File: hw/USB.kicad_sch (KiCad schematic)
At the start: 3 parts

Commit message: setup components information
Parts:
- R? (x2): footprint (none) -> Resistor_SMD:R_0805_2012Metric_Pad1.20x1.40mm_HandSolder; LCSC (none) -> C27834; Vendor (none) -> UNI-ROYAL(厚声); Vendor Model (none) -> 0805W8F5101T5E
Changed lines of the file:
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@@
       (effects (font (size 1.27 1.27)))
     )
-    (property "Footprint" "" (at 196.85 75.438 90)
+    (property "Footprint" "Resistor_SMD:R_0805_2012Metric_Pad1.20x1.40mm_HandSolder" (at 196.85 75.438 90)
       (effects (font (size 1.27 1.27)) hide)
     )
     (property "Datasheet" "~" (at 196.85 73.66 0)
+      (effects (font (size 1.27 1.27)) hide)
+    )
+    (property "Description" "电阻类型: 厚膜电阻 阻值: 5.1kΩ 精度: ±1% 功率: 1/8W 温度系数: ±100ppm/℃ 最大工作电压: 150V 工作温度" (at 196.85 73.66 0)
+      (effects (font (size 1.27 1.27)) hide)
+    )
+    (property "LCSC" "C27834" (at 196.85 73.66 0)
+      (effects (font (size 1.27 1.27)) hide)
+    )
+    (property "Vendor" "UNI-ROYAL(厚声)" (at 196.85 73.66 0)
+      (effects (font (size 1.27 1.27)) hide)
+    )
+    (property "Vendor Model" "0805W8F5101T5E" (at 196.85 73.66 0)
       (effects (font (size 1.27 1.27)) hide)
     )
@@
       (effects (font (size 1.27 1.27)))
     )
-    (property "Footprint" "" (at 196.85 88.138 90)
+    (property "Footprint" "Resistor_SMD:R_0805_2012Metric_Pad1.20x1.40mm_HandSolder" (at 196.85 88.138 90)
       (effects (font (size 1.27 1.27)) hide)
     )
@@
       (effects (font (size 1.27 1.27)) hide)
     )
+    (property "Description" "电阻类型: 厚膜电阻 阻值: 5.1kΩ 精度: ±1% 功率: 1/8W 温度系数: ±100ppm/℃ 最大工作电压: 150V 工作温度" (at 196.85 86.36 0)
+      (effects (font (size 1.27 1.27)) hide)
+    )
+    (property "LCSC" "C27834" (at 196.85 86.36 0)
+      (effects (font (size 1.27 1.27)) hide)
+    )
+    (property "Vendor" "UNI-ROYAL(厚声)" (at 196.85 86.36 0)
+      (effects (font (size 1.27 1.27)) hide)
+    )
+    (property "Vendor Model" "0805W8F5101T5E" (at 196.85 86.36 0)
+      (effects (font (size 1.27 1.27)) hide)
+    )

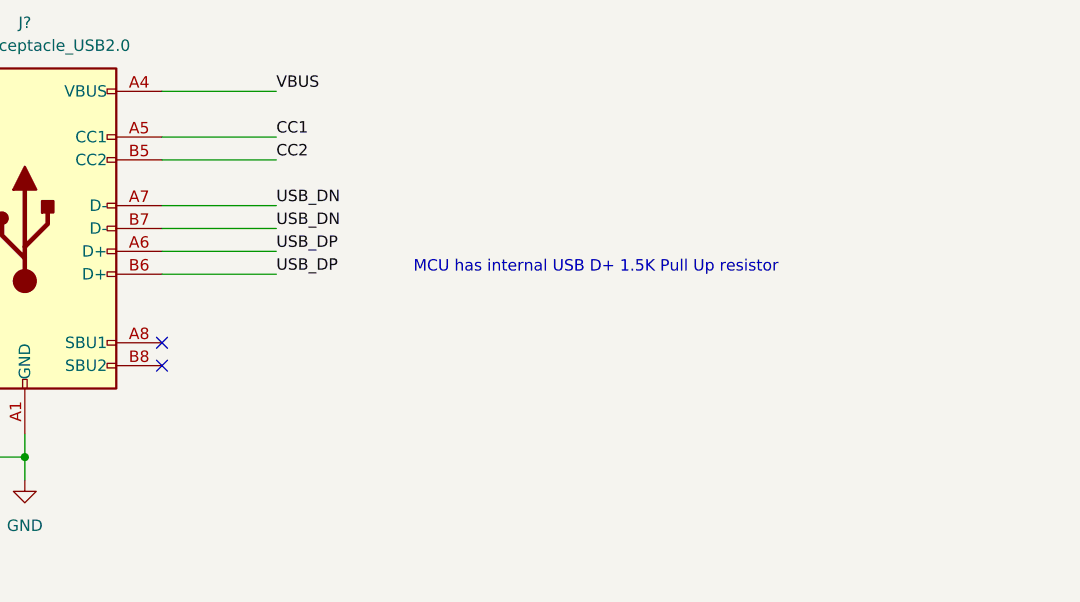
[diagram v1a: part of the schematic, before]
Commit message: added ESD for USB
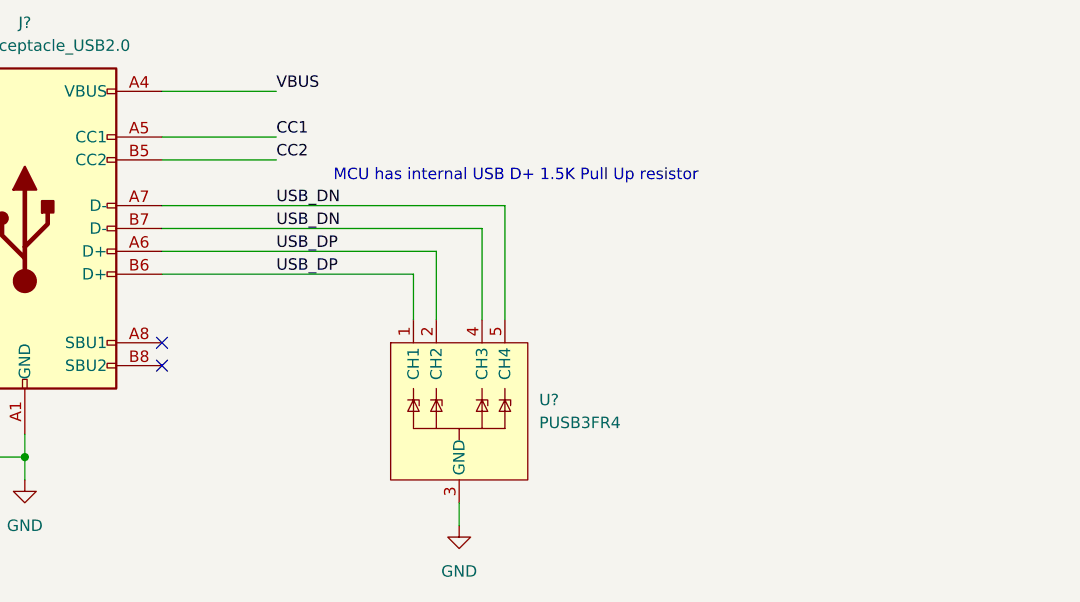
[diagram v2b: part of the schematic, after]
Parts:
- added U?: PUSB3FR4, symbol IotPi_Power_Protections:PUSB3FR4
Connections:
- net GND: now also U?.3 (GND), U?.8 (GND)
- net USB_DN: now also U?.4 (CH3), U?.5 (CH4)
- net USB_DP: now also U?.1 (CH1), U?.2 (CH2)
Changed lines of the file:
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@@
     (stroke (width 0) (type default))
   )
-  (wire (pts (xy 63.5 83.82) (xy 76.2 83.82))
+  (wire (pts (xy 63.5 83.82) (xy 93.98 83.82))
     (stroke (width 0) (type default))
   )
@@
     (stroke (width 0) (type default))
   )
+  (wire (pts (xy 63.5 81.28) (xy 99.06 81.28))
+    (stroke (width 0) (type default))
+  )
+  (wire (pts (xy 63.5 78.74) (xy 101.6 78.74))
+    (stroke (width 0) (type default))
+  )
+  (wire (pts (xy 101.6 91.44) (xy 101.6 78.74))
+    (stroke (width 0) (type default))
+  )
   (wire (pts (xy 40.64 104.14) (xy 40.64 106.68))
     (stroke (width 0) (type default))
@@
     (stroke (width 0) (type default))
   )
-  (wire (pts (xy 63.5 78.74) (xy 76.2 78.74))
+  (wire (pts (xy 91.44 91.44) (xy 91.44 86.36))
+    (stroke (width 0) (type default))
+  )
+  (wire (pts (xy 96.52 111.76) (xy 96.52 114.3))
+    (stroke (width 0) (type default))
+  )
+  (wire (pts (xy 99.06 91.44) (xy 99.06 81.28))
     (stroke (width 0) (type default))
   )
@@
     (stroke (width 0) (type default))
   )
-  (wire (pts (xy 63.5 86.36) (xy 76.2 86.36))
-    (stroke (width 0) (type default))
-  )
   (wire (pts (xy 33.02 22.86) (xy 45.72 22.86))
     (stroke (width 0) (type default))
@@
     (stroke (width 0) (type default))
   )
+  (wire (pts (xy 63.5 86.36) (xy 91.44 86.36))
+    (stroke (width 0) (type default))
+  )
   (wire (pts (xy 63.5 66.04) (xy 76.2 66.04))
     (stroke (width 0) (type default))
   )
-  (wire (pts (xy 63.5 81.28) (xy 76.2 81.28))
-    (stroke (width 0) (type default))
-  )
-  (text "MCU has internal USB D+ 1.5K Pull Up resistor" (at 91.44 86.36 0)
+  (wire (pts (xy 93.98 91.44) (xy 93.98 83.82))
+    (stroke (width 0) (type default))
+  )
+  (text "MCU has internal USB D+ 1.5K Pull Up resistor" (at 82.55 76.2 0)
     (effects (font (size 1.27 1.27)) (justify left bottom))
   )
@@
     )
   )
+  (symbol (lib_id "IotPi_Power_Protections:PUSB3FR4") (at 96.52 101.6 0) (unit 1)
+    (in_bom yes) (on_board yes) (dnp no) (fields_autoplaced)
+    (property "Reference" "U?" (at 105.41 100.33 0)
+      (effects (font (size 1.27 1.27)) (justify left))
+    )
+    (property "Value" "PUSB3FR4" (at 105.41 102.87 0)
+      (effects (font (size 1.27 1.27)) (justify left))
+    )
+    (property "Footprint" "" (at 96.52 101.6 0)
+      (effects (font (size 1.27 1.27)) hide)
+    )
+    (property "Datasheet" "" (at 96.52 101.6 0)
+      (effects (font (size 1.27 1.27)) hide)
+    )
+    (pin "1")
+    (pin "10")
+    (pin "2")
+    (pin "3")
+    (pin "4")
+    (pin "5")
+    (pin "6")
+    (pin "7")
+    (pin "8")
+    (pin "9")
+    (instances
+      (project "KiConSZ2023"
+        (path "/8659c260-f029-4e72-8b9a-85fff45eea40/8c3d77ce-3286-43c7-9eb6-2cc129677791"
+          (reference "U?") (unit 1)
+        )
+      )
+    )
+  )
   (symbol (lib_id "Device:R") (at 196.85 86.36 90) (unit 1)
     (in_bom yes) (on_board yes) (dnp no)
@@
         )
       )
+    )
+  )
+  (symbol (lib_id "power:GND") (at 96.52 114.3 0) (unit 1)
+    (in_bom yes) (on_board yes) (dnp no) (fields_autoplaced)
+    (property "Reference" "#PWR05803" (at 96.52 120.65 0)
+      (effects (font (size 1.27 1.27)) hide)
+    )
+    (property "Value" "GND" (at 96.52 119.38 0)
+      (effects (font (size 1.27 1.27)))
+    )
+    (property "Footprint" "" (at 96.52 114.3 0)
+      (effects (font (size 1.27 1.27)) hide)
+    )
+    (property "Datasheet" "" (at 96.52 114.3 0)
+      (effects (font (size 1.27 1.27)) hide)
+    )
+    (pin "1")
+    (instances
+      (project "KiConSZ2023"
+        (path "/8659c260-f029-4e72-8b9a-85fff45eea40/8c3d77ce-3286-43c7-9eb6-2cc129677791"
+          (reference "#PWR05803") (unit 1)
+        )
+      )

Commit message: added switches
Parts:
- U?: footprint (none) -> IotPi_Package_DFN_QFN:Nexperia_DFN2510A-10
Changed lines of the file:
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@@
   (symbol (lib_id "power:GND") (at 210.82 91.44 0) (unit 1)
     (in_bom yes) (on_board yes) (dnp no) (fields_autoplaced)
-    (property "Reference" "#PWR05802" (at 210.82 97.79 0)
+    (property "Reference" "#PWR?" (at 210.82 97.79 0)
       (effects (font (size 1.27 1.27)) hide)
     )
@@
       (project "KiConSZ2023"
         (path "/8659c260-f029-4e72-8b9a-85fff45eea40/8c3d77ce-3286-43c7-9eb6-2cc129677791"
-          (reference "#PWR05802") (unit 1)
+          (reference "#PWR?") (unit 1)
         )
       )
@@
   (symbol (lib_id "power:GND") (at 48.26 109.22 0) (unit 1)
     (in_bom yes) (on_board yes) (dnp no) (fields_autoplaced)
-    (property "Reference" "#PWR05801" (at 48.26 115.57 0)
+    (property "Reference" "#PWR?" (at 48.26 115.57 0)
       (effects (font (size 1.27 1.27)) hide)
     )
@@
       (project "KiConSZ2023"
         (path "/8659c260-f029-4e72-8b9a-85fff45eea40/8c3d77ce-3286-43c7-9eb6-2cc129677791"
-          (reference "#PWR05801") (unit 1)
+          (reference "#PWR?") (unit 1)
         )
       )
@@
       (effects (font (size 1.27 1.27)) (justify left))
     )
-    (property "Footprint" "" (at 96.52 101.6 0)
+    (property "Footprint" "IotPi_Package_DFN_QFN:Nexperia_DFN2510A-10" (at 96.52 101.6 0)
       (effects (font (size 1.27 1.27)) hide)
     )
@@
   (symbol (lib_id "power:GND") (at 96.52 114.3 0) (unit 1)
     (in_bom yes) (on_board yes) (dnp no) (fields_autoplaced)
-    (property "Reference" "#PWR05803" (at 96.52 120.65 0)
+    (property "Reference" "#PWR?" (at 96.52 120.65 0)
       (effects (font (size 1.27 1.27)) hide)
     )
@@
       (project "KiConSZ2023"
         (path "/8659c260-f029-4e72-8b9a-85fff45eea40/8c3d77ce-3286-43c7-9eb6-2cc129677791"
-          (reference "#PWR05803") (unit 1)
+          (reference "#PWR?") (unit 1)
         )
       )

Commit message: annotations
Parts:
- gave numbers to parts that had none: 4
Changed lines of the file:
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@@
   (symbol (lib_id "Device:R") (at 196.85 73.66 90) (unit 1)
     (in_bom yes) (on_board yes) (dnp no)
-    (property "Reference" "R?" (at 196.85 67.31 90)
+    (property "Reference" "R148" (at 196.85 67.31 90)
       (effects (font (size 1.27 1.27)))
     )
@@
       (project "KiConSZ2023"
         (path "/8659c260-f029-4e72-8b9a-85fff45eea40/8c3d77ce-3286-43c7-9eb6-2cc129677791"
-          (reference "R?") (unit 1)
+          (reference "R148") (unit 1)
         )
       )
@@
   (symbol (lib_id "power:GND") (at 210.82 91.44 0) (unit 1)
     (in_bom yes) (on_board yes) (dnp no) (fields_autoplaced)
-    (property "Reference" "#PWR?" (at 210.82 97.79 0)
+    (property "Reference" "#PWR08" (at 210.82 97.79 0)
       (effects (font (size 1.27 1.27)) hide)
     )
@@
       (project "KiConSZ2023"
         (path "/8659c260-f029-4e72-8b9a-85fff45eea40/8c3d77ce-3286-43c7-9eb6-2cc129677791"
-          (reference "#PWR?") (unit 1)
+          (reference "#PWR08") (unit 1)
         )
       )
@@
   (symbol (lib_id "power:GND") (at 48.26 109.22 0) (unit 1)
     (in_bom yes) (on_board yes) (dnp no) (fields_autoplaced)
-    (property "Reference" "#PWR?" (at 48.26 115.57 0)
+    (property "Reference" "#PWR06" (at 48.26 115.57 0)
       (effects (font (size 1.27 1.27)) hide)
     )
@@
       (project "KiConSZ2023"
         (path "/8659c260-f029-4e72-8b9a-85fff45eea40/8c3d77ce-3286-43c7-9eb6-2cc129677791"
-          (reference "#PWR?") (unit 1)
+          (reference "#PWR06") (unit 1)
         )
       )
@@
   (symbol (lib_id "Connector:USB_C_Receptacle_USB2.0") (at 48.26 81.28 0) (unit 1)
     (in_bom yes) (on_board yes) (dnp no) (fields_autoplaced)
-    (property "Reference" "J?" (at 48.26 58.42 0)
+    (property "Reference" "J2" (at 48.26 58.42 0)
       (effects (font (size 1.27 1.27)))
     )
@@
       (project "KiConSZ2023"
         (path "/8659c260-f029-4e72-8b9a-85fff45eea40/8c3d77ce-3286-43c7-9eb6-2cc129677791"
-          (reference "J?") (unit 1)
+          (reference "J2") (unit 1)
         )
       )
@@
   (symbol (lib_id "IotPi_Power_Protections:PUSB3FR4") (at 96.52 101.6 0) (unit 1)
     (in_bom yes) (on_board yes) (dnp no) (fields_autoplaced)
-    (property "Reference" "U?" (at 105.41 100.33 0)
+    (property "Reference" "U3" (at 105.41 100.33 0)
       (effects (font (size 1.27 1.27)) (justify left))
     )
@@
       (project "KiConSZ2023"
         (path "/8659c260-f029-4e72-8b9a-85fff45eea40/8c3d77ce-3286-43c7-9eb6-2cc129677791"
-          (reference "U?") (unit 1)
+          (reference "U3") (unit 1)
         )
       )
@@
   (symbol (lib_id "Device:R") (at 196.85 86.36 90) (unit 1)
     (in_bom yes) (on_board yes) (dnp no)
-    (property "Reference" "R?" (at 196.85 80.01 90)
+    (property "Reference" "R149" (at 196.85 80.01 90)
       (effects (font (size 1.27 1.27)))
     )
@@
       (project "KiConSZ2023"
         (path "/8659c260-f029-4e72-8b9a-85fff45eea40/8c3d77ce-3286-43c7-9eb6-2cc129677791"
-          (reference "R?") (unit 1)
+          (reference "R149") (unit 1)
         )
       )
@@
   (symbol (lib_id "power:GND") (at 96.52 114.3 0) (unit 1)
     (in_bom yes) (on_board yes) (dnp no) (fields_autoplaced)
-    (property "Reference" "#PWR?" (at 96.52 120.65 0)
+    (property "Reference" "#PWR07" (at 96.52 120.65 0)
       (effects (font (size 1.27 1.27)) hide)
     )
@@
       (project "KiConSZ2023"
         (path "/8659c260-f029-4e72-8b9a-85fff45eea40/8c3d77ce-3286-43c7-9eb6-2cc129677791"
-          (reference "#PWR?") (unit 1)
-        )
-      )
+          (reference "#PWR07") (unit 1)
+        )
+      )

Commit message: updated LCSC of switches
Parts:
- U3: LCSC (none) -> C503418; Vendor (none) -> Nexperia(安世); Vendor Model (none) -> PUSB3FR4Z
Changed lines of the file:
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@@
+      (effects (font (size 1.27 1.27)) hide)
+    )
+    (property "Description" "单向通道数: 4 反向截止电压(Vrwm): 3.3V@Max 击穿电压: 5.5V 峰值脉冲电流(Ipp)@10/1000us: - 最大钳位电压:" (at 96.52 101.6 0)
+      (effects (font (size 1.27 1.27)) hide)
+    )
+    (property "LCSC" "C503418" (at 96.52 101.6 0)
+      (effects (font (size 1.27 1.27)) hide)
+    )
+    (property "Vendor" "Nexperia(安世)" (at 96.52 101.6 0)
+      (effects (font (size 1.27 1.27)) hide)
+    )
+    (property "Vendor Model" "PUSB3FR4Z" (at 96.52 101.6 0)
       (effects (font (size 1.27 1.27)) hide)
     )

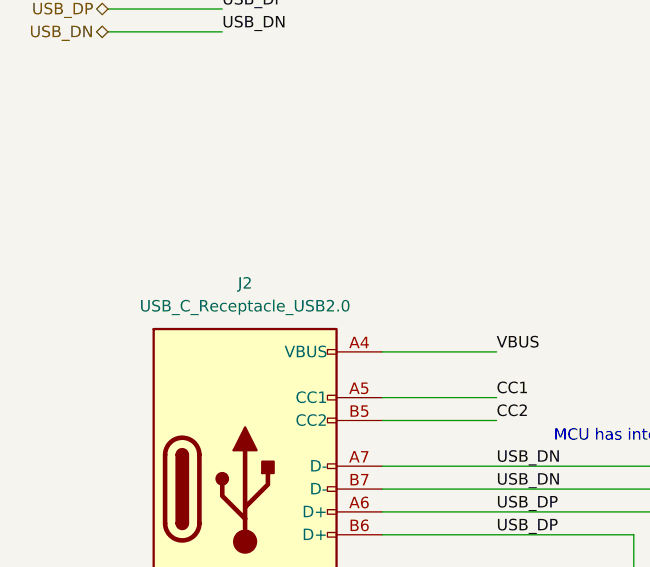
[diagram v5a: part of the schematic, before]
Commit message: fix issues in schematic and footprints
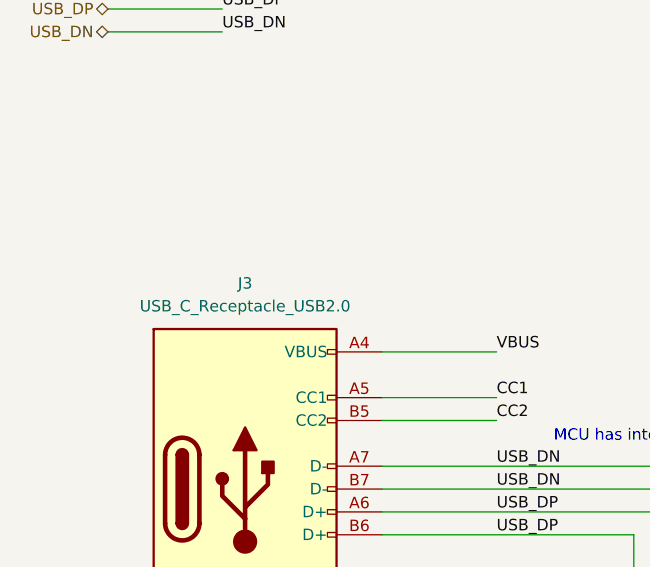
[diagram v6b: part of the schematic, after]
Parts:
- renumbered J2 to J3
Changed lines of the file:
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@@
   (symbol (lib_id "Connector:USB_C_Receptacle_USB2.0") (at 48.26 81.28 0) (unit 1)
     (in_bom yes) (on_board yes) (dnp no) (fields_autoplaced)
-    (property "Reference" "J2" (at 48.26 58.42 0)
+    (property "Reference" "J3" (at 48.26 58.42 0)
       (effects (font (size 1.27 1.27)))
     )
@@
       (project "KiConSZ2023"
         (path "/8659c260-f029-4e72-8b9a-85fff45eea40/8c3d77ce-3286-43c7-9eb6-2cc129677791"
-          (reference "J2") (unit 1)
+          (reference "J3") (unit 1)
         )
       )

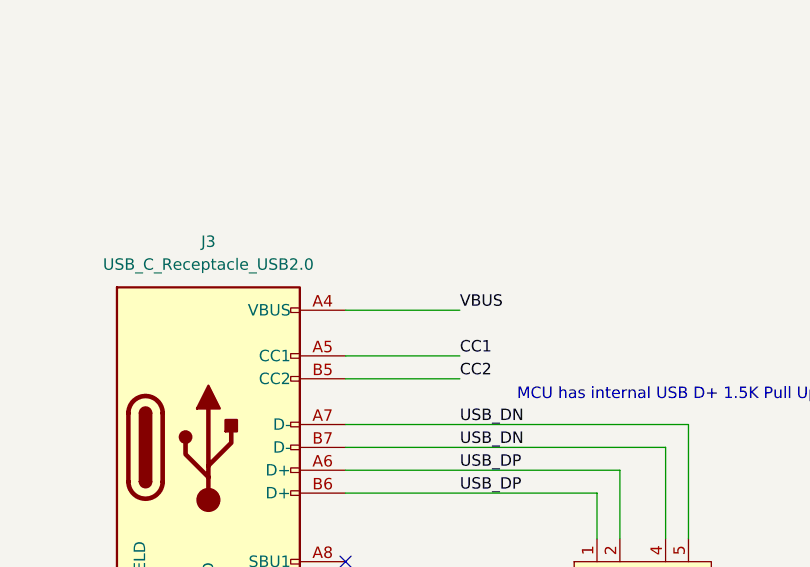
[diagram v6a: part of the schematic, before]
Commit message: updated and fix ERCs
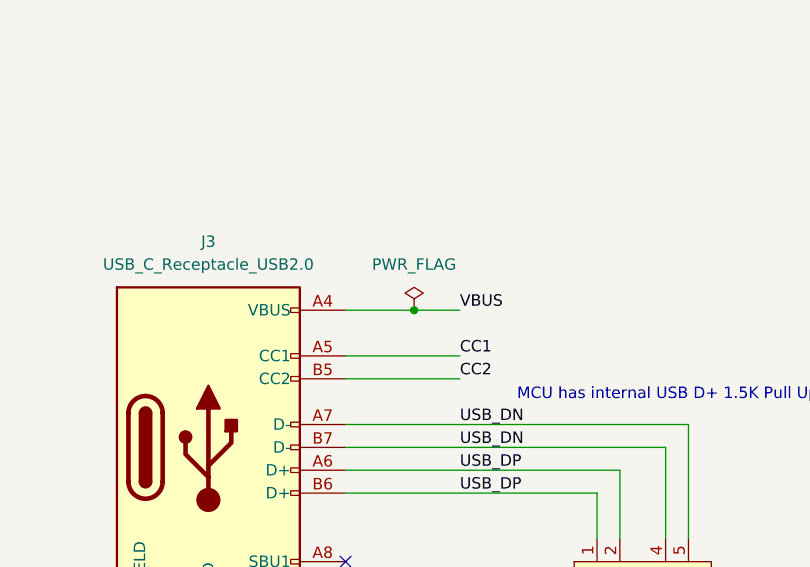
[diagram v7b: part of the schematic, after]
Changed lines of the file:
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@@
 (kicad_sch (version 20230121) (generator eeschema)
   (paper "A4")
+  (junction (at 71.12 66.04) (diameter 0) (color 0 0 0 0)
+  )
   (junction (at 210.82 86.36) (diameter 0) (color 0 0 0 0)
   )
@@
     (stroke (width 0) (type default))
   )
+  (wire (pts (xy 71.12 66.04) (xy 76.2 66.04))
+    (stroke (width 0) (type default))
+  )
   (wire (pts (xy 96.52 111.76) (xy 96.52 114.3))
     (stroke (width 0) (type default))
@@
     (stroke (width 0) (type default))
   )
-  (wire (pts (xy 63.5 66.04) (xy 76.2 66.04))
+  (wire (pts (xy 63.5 66.04) (xy 71.12 66.04))
     (stroke (width 0) (type default))
   )
@@
         )
       )
+    )
+  )
+  (symbol (lib_id "power:PWR_FLAG") (at 71.12 66.04 0) (unit 1)
+    (in_bom yes) (on_board yes) (dnp no) (fields_autoplaced)
+    (property "Reference" "#FLG03" (at 71.12 64.135 0)
+      (effects (font (size 1.27 1.27)) hide)
+    )
+    (property "Value" "PWR_FLAG" (at 71.12 60.96 0)
+      (effects (font (size 1.27 1.27)))
+    )
+    (property "Footprint" "" (at 71.12 66.04 0)
+      (effects (font (size 1.27 1.27)) hide)
+    )
+    (property "Datasheet" "~" (at 71.12 66.04 0)
+      (effects (font (size 1.27 1.27)) hide)
+    )
+    (pin "1")
+    (instances
+      (project "KiConSZ2023"
+        (path "/8659c260-f029-4e72-8b9a-85fff45eea40/8c3d77ce-3286-43c7-9eb6-2cc129677791"
+          (reference "#FLG03") (unit 1)
+        )
+      )
